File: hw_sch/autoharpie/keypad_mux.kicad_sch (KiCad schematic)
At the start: 2 parts, among them U10 74LVC1G139

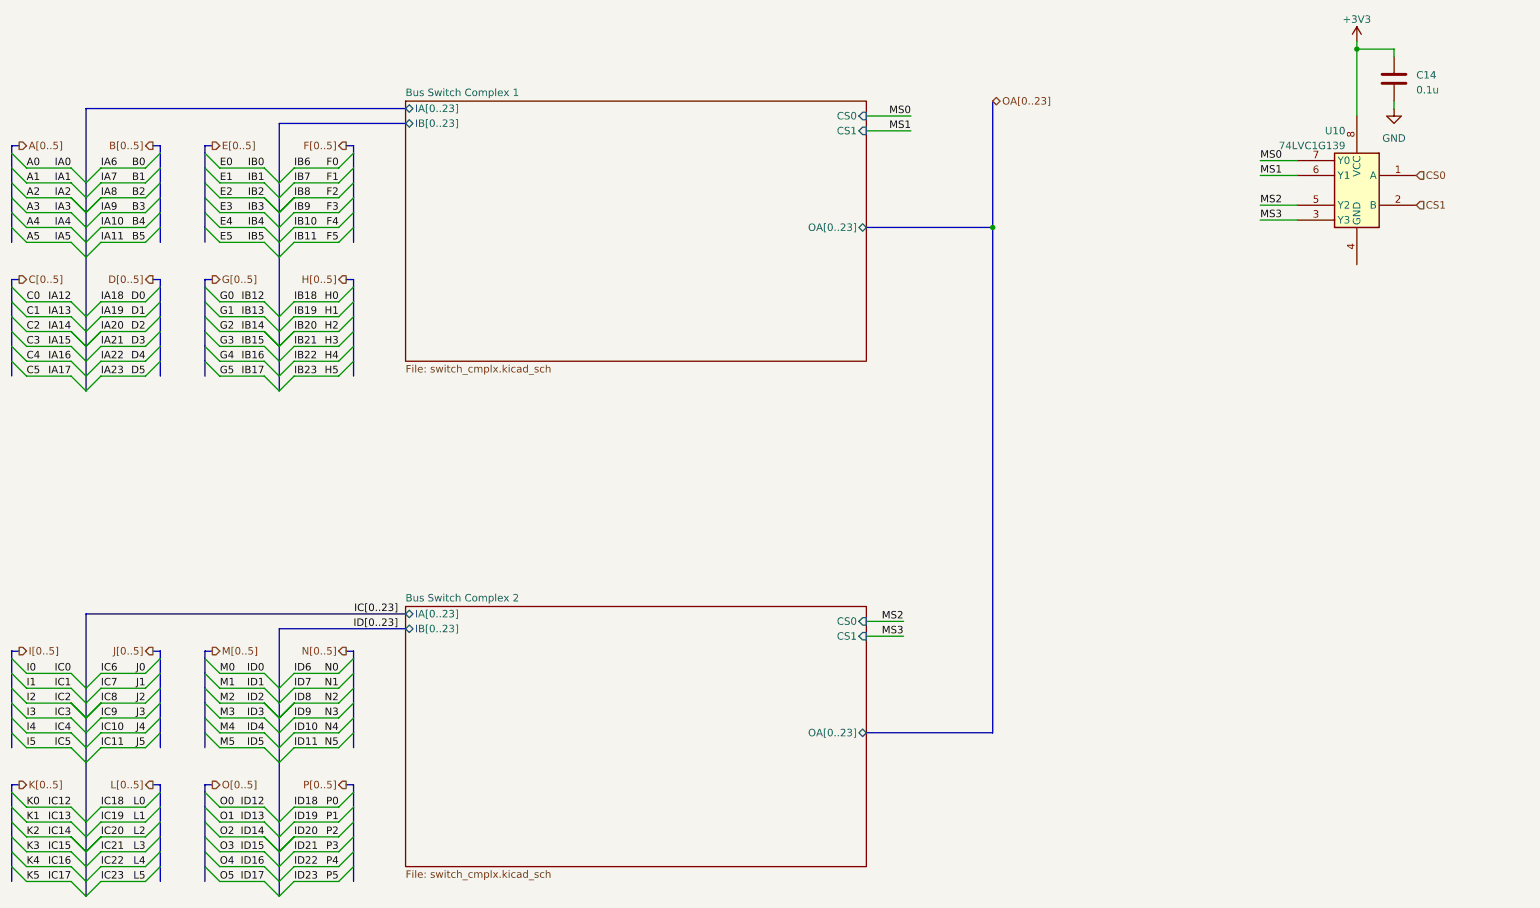
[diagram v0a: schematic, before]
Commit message: switch to teensy reduce pins
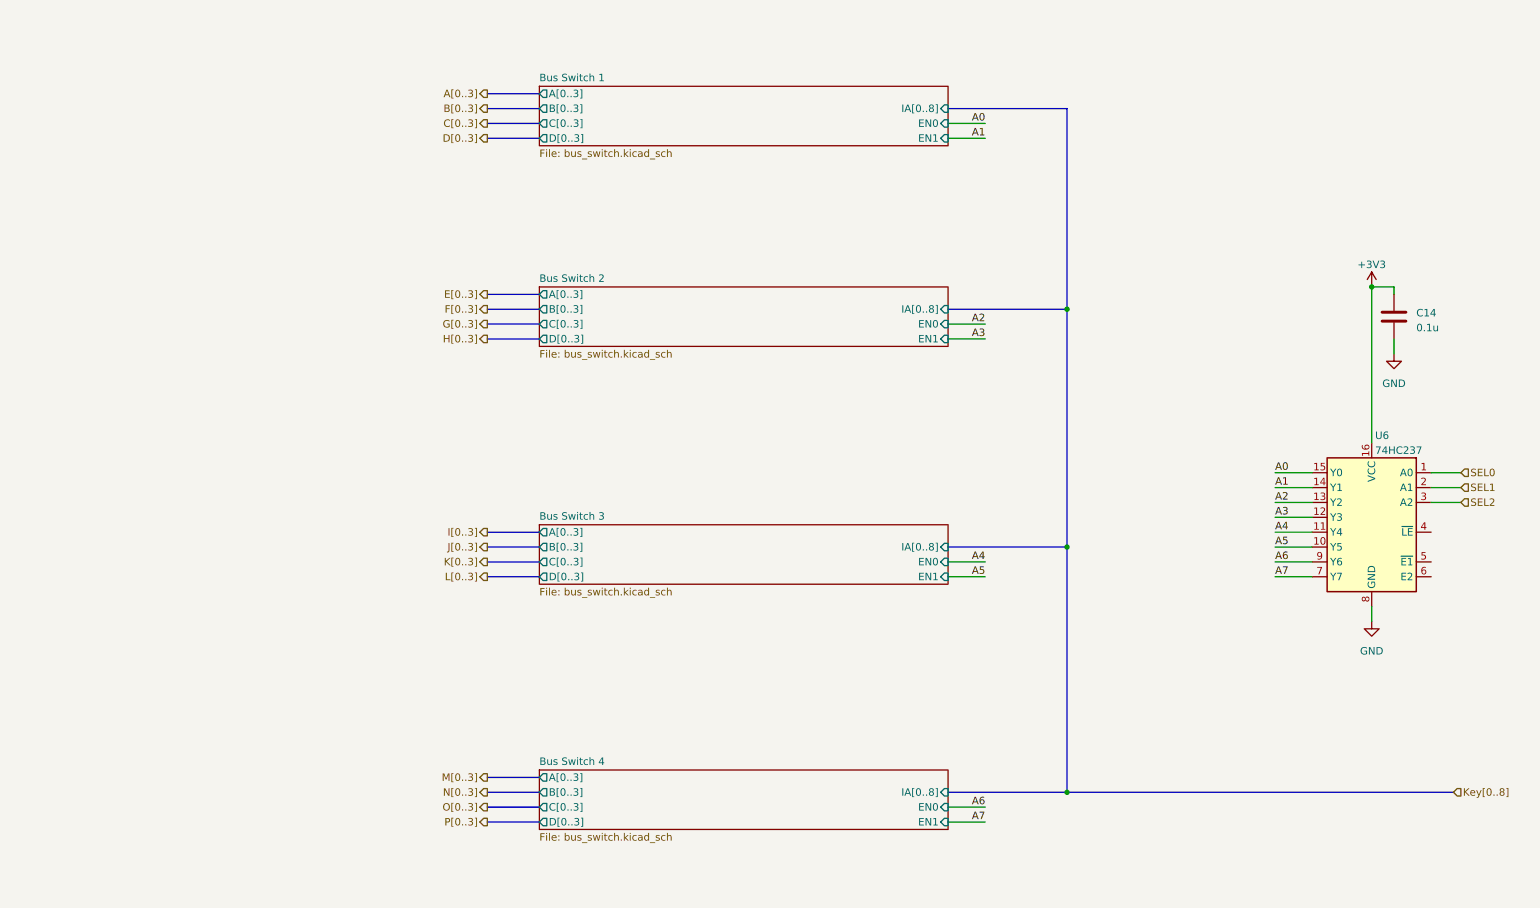
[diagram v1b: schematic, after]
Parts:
- removed U10: 74LVC1G139, symbol 74xGxx:74LVC1G139
- added U6: 74HC237, symbol 74xx:74HC237
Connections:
- net +3V3: now also U6.16 (VCC)
- net A0: now also U6.15 (Y0)
- net A1: now also U6.14 (Y1)
- net A2: now also U6.13 (Y2)
- net A3: now also U6.12 (Y3)
- net A4: now also U6.11 (Y4)
- net A5: now also U6.10 (Y5)
- net GND: now also U6.8 (GND)
- new net A6: U6.9 (Y6)
- new net A7: U6.7 (Y7)
- new net SEL0: U6.1 (A0)
- new net SEL1: U6.2 (A1)
- new net SEL2: U6.3 (A2)
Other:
- removed sheet Bus Switch Complex 1
- removed sheet Bus Switch Complex 2
- added sheet Bus Switch 1 (bus_switch.kicad_sch)
- added sheet Bus Switch 2 (bus_switch.kicad_sch)
- added sheet Bus Switch 3 (bus_switch.kicad_sch)
- added sheet Bus Switch 4 (bus_switch.kicad_sch)
